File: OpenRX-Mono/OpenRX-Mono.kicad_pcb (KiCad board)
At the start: 2 copper layers, 45 parts, among them T1 0900PC16J0042001E, U1 ESP32-C3FH4, U2 TLV75533PDQNR, U3 RFX2401C, U4 LR1121IMLTRT, U5 OW2EL89CENUXFMYLC-32M, X1 CJ17-400001010B20

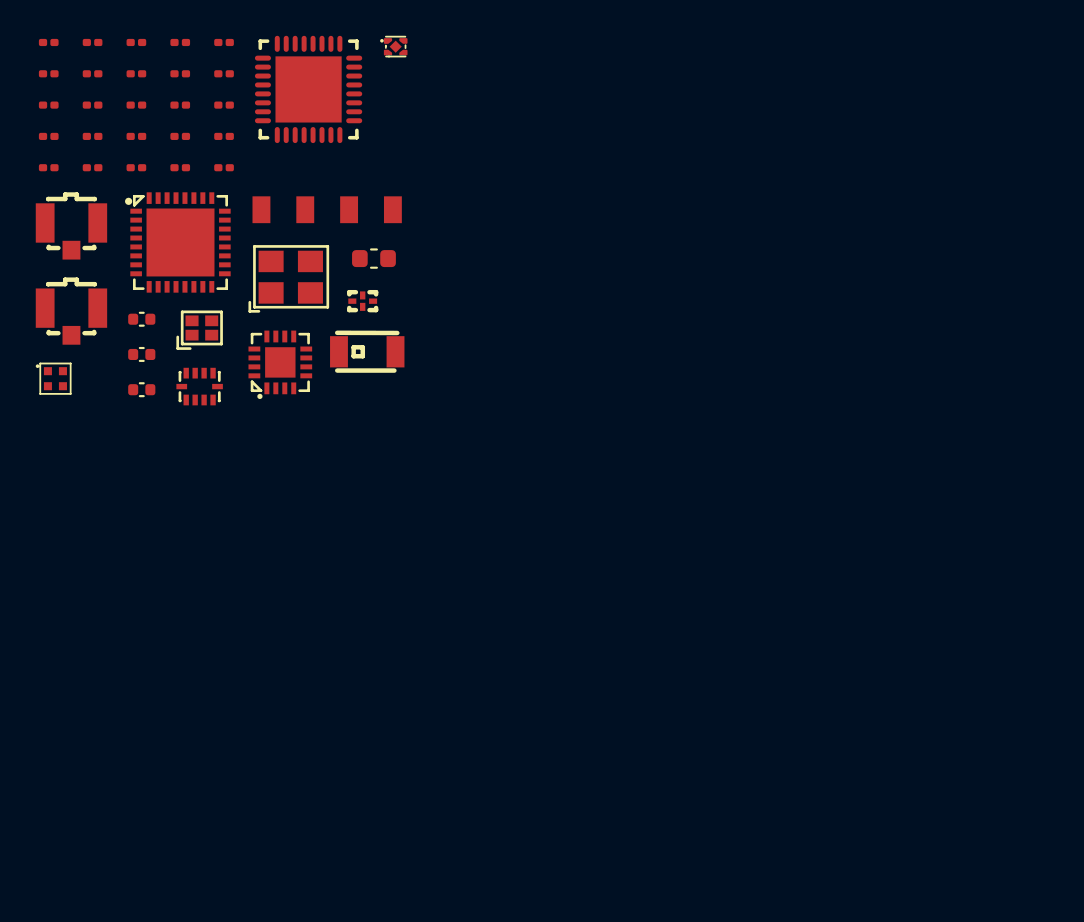
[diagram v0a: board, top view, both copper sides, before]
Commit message: Gemini: copy Mono schematic as base for dual-radio build
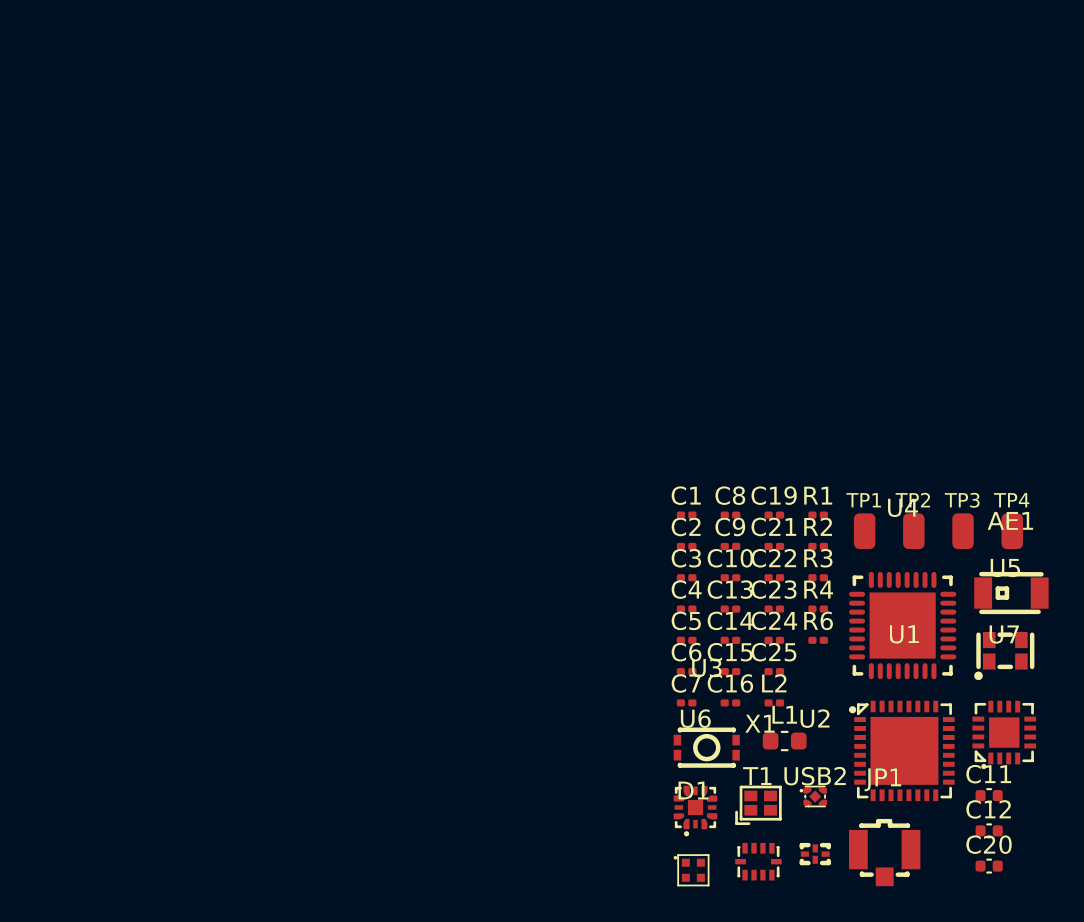
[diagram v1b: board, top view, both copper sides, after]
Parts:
- removed C26: 1uF, Capacitor_SMD:C_0201_0603Metric
- removed JP2: U.FL-R-SMT-1(80), OpenRX-Shared:RF-SMD_FRF05002-JSS103M
- removed R5, R7: 100k, Resistor_SMD:R_0201_0603Metric
- removed USB1: DEA102700LT-6307A2, OpenRX-Shared:FILTER-SMD_4P-L1.0-W0.5-L_DEA102700LT-XXX
- added C14: 1uF, Capacitor_SMD:C_0201_0603Metric, F.Cu at (133.8, 91.4)
- added C15: 220pF, Capacitor_SMD:C_0201_0603Metric, F.Cu at (133.8, 93.1)
- added C16: 0.3pF, Capacitor_SMD:C_0201_0603Metric, F.Cu at (133.8, 94.9)
- added L2: 24nH, Inductor_SMD:L_0201_0603Metric, F.Cu at (136.3, 94.9)
- added U6: SKY13588-460LF, OpenRX-Shared:QFN-12_L2.0-W2.0-P0.50-BL-EP0.8, F.Cu at (131.9, 100.7)
- added U7: RFX2401C, OpenRX-Shared:QFN-16_L3.0-W3.0-P0.50-BL-EP1.7, F.Cu at (149.1, 96.5)
- added USB2: DEA102700LT-6307A2, OpenRX-Shared:FILTER-SMD_4P-L1.0-W0.5-L_DEA102700LT-XXX, F.Cu at (138.6, 103.3)
- C25: value 220pF -> 100nF
- TP1, TP2, TP3, TP4: footprint OpenRX-Shared:SolderPad_1.0x1.5mm -> OpenRX-Shared:SolderPad_1.2x2.0mm
- U3: value RFX2401C -> TS2306A 240GF MSM 9_C2976675; footprint OpenRX-Shared:QFN-16_L3.0-W3.0-P0.50-BL-EP1.7 -> OpenRX-Shared:SW-SMD_4P-L3.0-W2.0-P0.85-LS3.5
- U5: value OW2EL89CENUXFMYLC-32M -> OW7EL89CENUYO3YLC-32M; footprint OpenRX-Shared:OSC-SMD_4P-L3.2-W2.5-BL -> OpenRX-Shared:OSC-SMD_4P-L2.0-W1.6-BL_TXC_7Z
- moved JP1 57.4 mm to (142.4, 103.8)
- moved C11 54.3 mm to (148.3, 100.1)
- moved C12 54.3 mm to (148.3, 102.0)
- moved C20 54.3 mm to (148.3, 104.0)
- moved U1 49.5 mm to (143.6, 97.6)
- moved C6 48.4 mm to (131.4, 93.1)
- moved C7 48.4 mm to (131.4, 94.9)
- moved U2 48.0 mm to (138.6, 100.1)
- moved C24 47.1 mm to (136.3, 91.4)
- moved C25 47.1 mm to (136.3, 93.1)
- moved C13 45.9 mm to (133.8, 89.6)
- moved U5 45.1 mm to (149.2, 92.0)
- moved D1 45.0 mm to (131.8, 104.2)
- moved U4 44.7 mm to (143.4, 90.5)
- moved R3 44.7 mm to (138.7, 87.9)
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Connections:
- net /ESP32-C3 + LR1121 Mono/BUSY renamed /ESP32-C3 + LR1121 Mono/BUSY1
- net /ESP32-C3 + LR1121 Mono/RST renamed /ESP32-C3 + LR1121 Mono/RST1
- C23 pad 1: Net-(U5-VDD) -> GND
- C6 pad 1: /ESP32-C3 + LR1121 Mono/XTAL_P -> Net-(C6-Pad1)
- R2 pad 2: /ESP32-C3 + LR1121 Mono/NSS -> /ESP32-C3 + LR1121 Mono/NSS1
- R3 pad 2: /ESP32-C3 + LR1121 Mono/CHIP_BOOT -> /ESP32-C3 + LR1121 Mono/BUTTON
- T1 pad 6: Net-(JP1-SIG) -> Net-(T1-RX)
- T1 pad 8: Net-(JP1-SIG) -> Net-(T1-RX)
- T1 pad 9: Net-(JP1-SIG) -> Net-(T1-RX)
- U1 pad 10: /ESP32-C3 + LR1121 Mono/DIO1 -> /ESP32-C3 + LR1121 Mono/MISO
- U1 pad 12: /ESP32-C3 + LR1121 Mono/MISO -> /ESP32-C3 + LR1121 Mono/SCK
- U1 pad 13: /ESP32-C3 + LR1121 Mono/MOSI -> /ESP32-C3 + LR1121 Mono/NSS1
- U1 pad 14: /ESP32-C3 + LR1121 Mono/NSS -> /ESP32-C3 + LR1121 Mono/LED
- U1 pad 15: /ESP32-C3 + LR1121 Mono/CHIP_BOOT -> /ESP32-C3 + LR1121 Mono/BUTTON
- U1 pad 16: /ESP32-C3 + LR1121 Mono/LED -> unconnected-(U1-GPIO10-Pad16)
- U1 pad 5: unconnected-(U1-XTAL_32K_N-Pad5) -> /ESP32-C3 + LR1121 Mono/IRQ1
- U1 pad 9: /ESP32-C3 + LR1121 Mono/SCK -> /ESP32-C3 + LR1121 Mono/MOSI
- U3 pad 1: GND -> /ESP32-C3 + LR1121 Mono/BUTTON
- U4 pad 10: Net-(U4-DIO8) -> /ESP32-C3 + LR1121 Mono/DIO8-1
- U4 pad 11: Net-(U4-DIO7) -> /ESP32-C3 + LR1121 Mono/DIO7-1
- U4 pad 24: /ESP32-C3 + LR1121 Mono/NSS -> /ESP32-C3 + LR1121 Mono/NSS1
- U4 pad 26: Net-(U3-TXRX) -> Net-(U4-RFIO_HF)
- U4 pad 9: /ESP32-C3 + LR1121 Mono/DIO1 -> /ESP32-C3 + LR1121 Mono/IRQ1
- U5 pad 4: Net-(U5-VDD) -> Net-(U4-VTCXO)
- X1 pad 1: /ESP32-C3 + LR1121 Mono/XTAL_P -> Net-(C6-Pad1)
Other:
- copper layers 2 -> 4

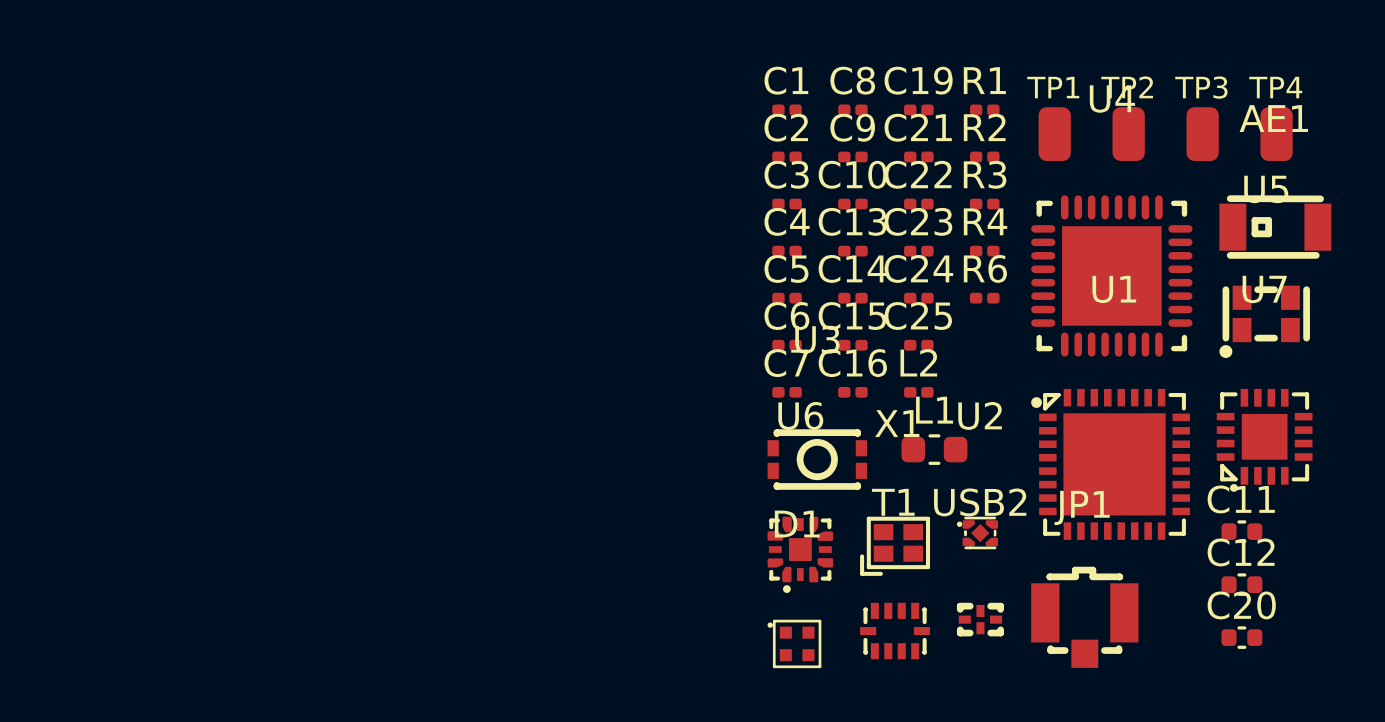
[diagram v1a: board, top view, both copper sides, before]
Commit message: Gemini: copy Mono schematic + PCB as starting point
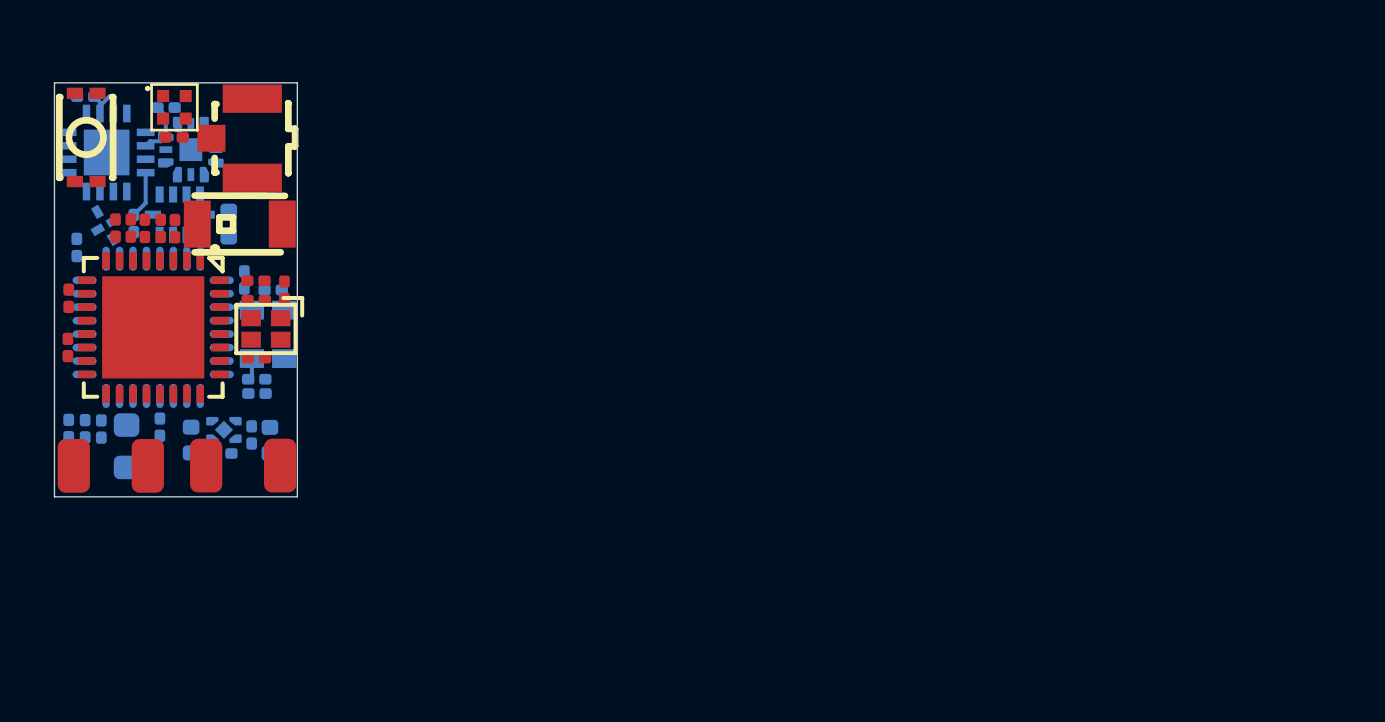
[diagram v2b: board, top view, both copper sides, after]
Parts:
- removed C25: 100nF, Capacitor_SMD:C_0201_0603Metric
- added C18: 100nF, Capacitor_SMD:C_0201_0603Metric, F.Cu at (108.6, 85.4)
- C10, C11, C12, C13, C14, C15, C16, C20, C21, C22, C23, C24, C3, C4, C9, L1, R2, R6, T1, U2, U4, U5, U6, U7, USB2: moved to B.Cu
- moved U7 44.3 mm to (106.1, 86.0), turned to 180 degrees
- moved C20 40.7 mm to (110.6, 88.6), turned to 90 degrees
- moved C12 39.4 mm to (109.2, 96.7), turned to 90 degrees
- moved TP3 39.0 mm to (109.8, 97.6)
- moved TP4 39.0 mm to (112.5, 97.6)
- moved AE1 38.5 mm to (111.0, 88.6)
- moved TP1 38.5 mm to (104.9, 97.6)
- moved TP2 38.5 mm to (107.6, 97.6)
- moved U5 37.1 mm to (112.1, 92.7), turned to -90 degrees
- moved JP1 36.7 mm to (110.7, 85.4), turned to -90 degrees
- moved C11 36.3 mm to (112.2, 96.7), turned to -90 degrees
- moved U1 36.1 mm to (107.8, 92.5), turned to -90 degrees
- moved U4 35.7 mm to (107.8, 92.5), turned to -90 degrees
- moved USB2 35.7 mm to (106.0, 88.7), turned to 120 degrees
- moved R3 34.5 mm to (104.6, 93.2), turned to -90 degrees
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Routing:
- net +3V3: track 0.00 -> 3.84 mm
- net Net-(U4-VTCXO): track 0.00 -> 2.11 mm
- net Net-(U6-J2): track 0.00 -> 1.68 mm
- net Net-(U5-OUTPUT): track 0.00 -> 0.83 mm
- net GND: track 0.00 -> 0.79 mm
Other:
- board outline added: 9 x 15.4 mm
